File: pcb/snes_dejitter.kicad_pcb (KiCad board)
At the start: 2 copper layers, 44.1 x 23.7 mm, 39 parts, among them J1 JTAG_CONN, J10 CSYNC_o, J2 5V, J3 GND, J4 GND, J5 CSYNC_i, J6 MCLK_EXT_i, J7 CLK_SEL_i, J8 GND, J9 MCLK_o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

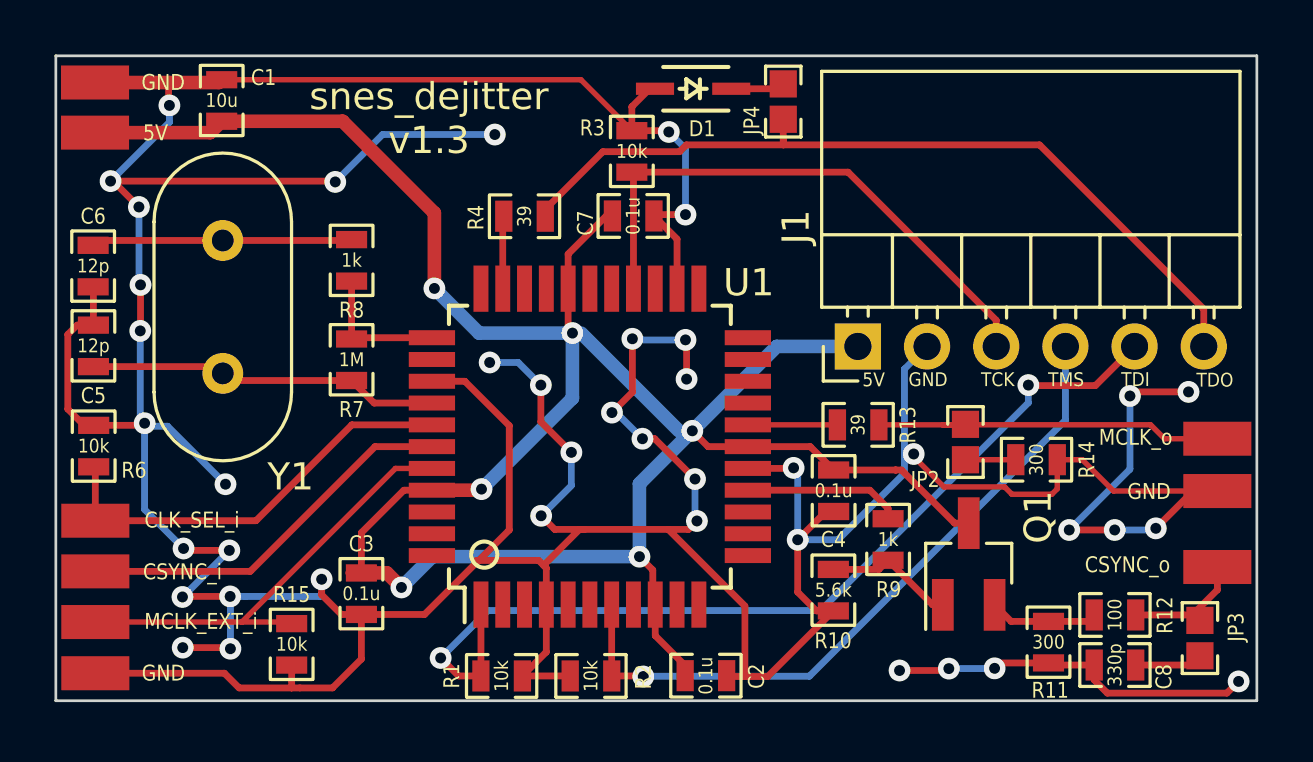
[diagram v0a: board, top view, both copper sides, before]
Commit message: update to ATF1502AS-10JU44
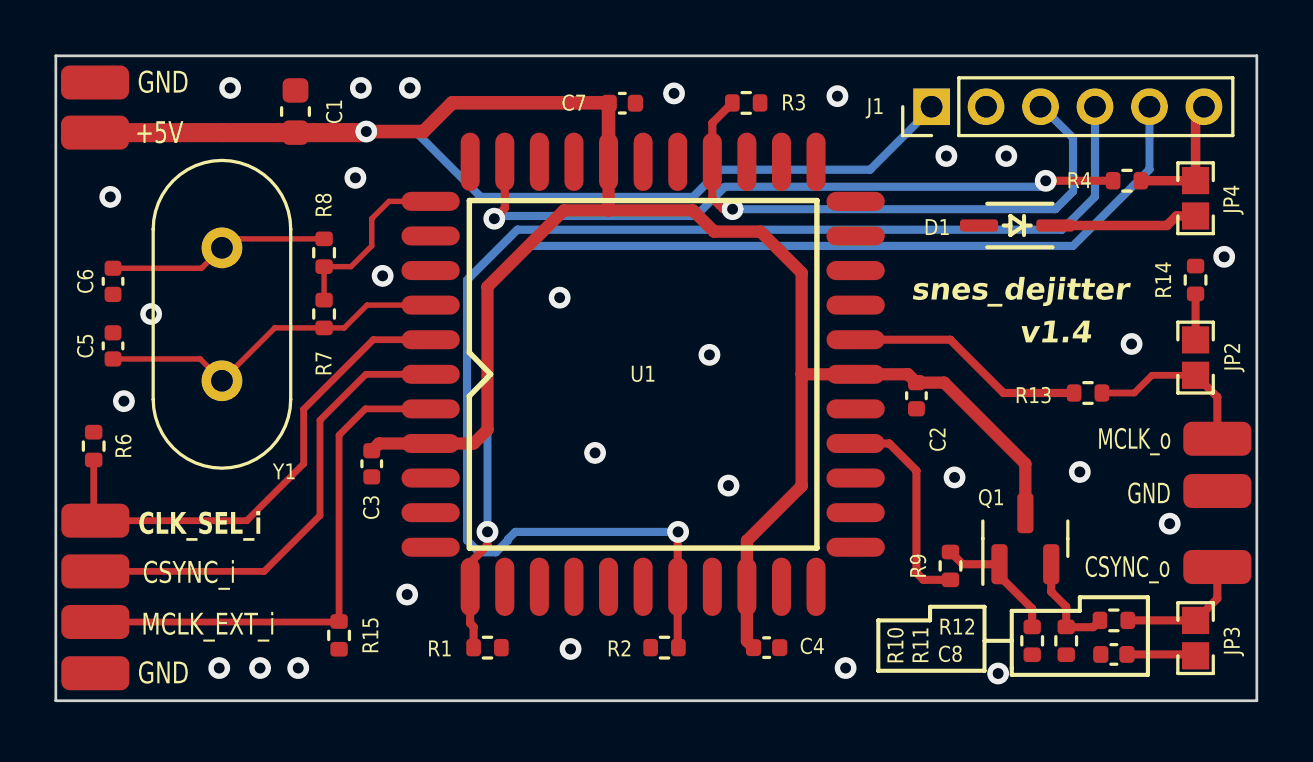
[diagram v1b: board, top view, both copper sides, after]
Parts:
- C1: footprint custom_components:SM0603_Capa_libcms -> Capacitor_SMD:C_0603_1608Metric
- C2, C3, C4, C5, C6, C7, C8: footprint custom_components:SM0603_Capa_libcms -> Capacitor_SMD:C_0402_1005Metric
- J1: footprint custom_components:JTAG_Header_Angled_1x06_Pitch2.54mm -> Connector_PinHeader_2.00mm:PinHeader_1x06_P2.00mm_Vertical
- J2: value 5V -> +5V
- Q1: footprint TO_SOT_Packages_SMD:SOT-23_Handsoldering -> Package_TO_SOT_SMD:SOT-23
- R1, R10, R11, R12, R13, R14, R15, R2, R3, R4, R6, R7, R8, R9: footprint custom_components:SM0603_Resistor_libcms -> Resistor_SMD:R_0402_1005Metric
- U1: footprint custom_components:TQFP-44_10x10mm_Pitch0.8mm_Handsoldering -> SamacSys_Parts:PLCC127P1753X1753X457-44N
- moved R4 22.2 mm to (52.2, 17.6)
- moved JP4 15.6 mm to (54.8, 18.2), turned to -90 degrees
- moved D1 12.9 mm to (48.2, 19.2)
- moved C2 12.9 mm to (44.5, 25.5), turned to -90 degrees
- moved J1 9.21 mm to (45.1, 14.9)
- moved JP2 9.00 mm to (54.8, 24.1), turned to 90 degrees
- moved R14 8.81 mm to (54.8, 21.2), turned to 90 degrees
- moved R13 8.52 mm to (50.8, 25.4)
- moved R10 7.53 mm to (48.8, 34.5)
- moved C4 6.26 mm to (39.0, 34.8), turned to 0 degrees
- moved C3 4.79 mm to (24.5, 28.0)
- moved R3 4.56 mm to (38.2, 14.8), turned to 0 degrees
- moved C7 4.16 mm to (33.7, 14.8)
- moved U1 3.30 mm to (34.5, 24.7)
- moved R2 2.89 mm to (35.2, 34.8)
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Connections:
- U1 pad 10: Net-(U1-Pad10) -> unconnected-(U1-Pad10)
- U1 pad 11: Net-(U1-Pad11) -> unconnected-(U1-Pad11)
- U1 pad 12: Net-(U1-Pad12) -> unconnected-(U1-Pad12)
- U1 pad 13: Net-(U1-Pad13) -> unconnected-(U1-Pad13)
- U1 pad 14: Net-(U1-Pad14) -> unconnected-(U1-Pad14)
- U1 pad 19: Net-(U1-Pad19) -> unconnected-(U1-Pad19)
- U1 pad 2: Net-(U1-Pad2) -> unconnected-(U1-Pad2)
- U1 pad 20: Net-(U1-Pad20) -> unconnected-(U1-Pad20)
- U1 pad 21: Net-(U1-Pad21) -> unconnected-(U1-Pad21)
- U1 pad 22: Net-(U1-Pad22) -> unconnected-(U1-Pad22)
- U1 pad 23: Net-(U1-Pad23) -> unconnected-(U1-Pad23)
- U1 pad 25: Net-(U1-Pad25) -> unconnected-(U1-Pad25)
- U1 pad 27: Net-(U1-Pad27) -> unconnected-(U1-Pad27)
- U1 pad 28: Net-(U1-Pad28) -> unconnected-(U1-Pad28)
- U1 pad 3: Net-(U1-Pad3) -> unconnected-(U1-Pad3)
- U1 pad 30: Net-(U1-Pad30) -> unconnected-(U1-Pad30)
- U1 pad 31: Net-(U1-Pad31) -> unconnected-(U1-Pad31)
- U1 pad 33: Net-(U1-Pad33) -> unconnected-(U1-Pad33)
- U1 pad 35: Net-(U1-Pad35) -> unconnected-(U1-Pad35)
- U1 pad 42: Net-(U1-Pad42) -> unconnected-(U1-Pad42)
- U1 pad 43: Net-(U1-Pad43) -> unconnected-(U1-Pad43)
- U1 pad 44: Net-(U1-Pad44) -> unconnected-(U1-Pad44)
- U1 pad 5: Net-(U1-Pad5) -> unconnected-(U1-Pad5)
- U1 pad 6: Net-(U1-Pad6) -> unconnected-(U1-Pad6)
- U1 pad 8: Net-(U1-Pad8) -> unconnected-(U1-Pad8)
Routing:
- net GND: track 230.1 -> 0.00 mm, vias 41 -> 28
- net Net-(J1-Pad6): track 30.2 -> 4.95 mm
- net /TMS: track 25.9 -> 49.7 mm
- net /TDO: track 2.68 -> 25.5 mm, vias 0 -> 2
- net /DVDD5V: track 88.4 -> 96.0 mm, vias 6 -> 1
- net Net-(R13-Pad1): track 13.5 -> 6.37 mm
- net /TDI: track 35.0 -> 42.0 mm, vias 2 -> 1
- net /GCLK_o: track 3.29 -> 8.83 mm
- net Net-(JP4-Pad2): track 1.98 -> 5.54 mm
- net /CSYNC_i: track 14.3 -> 17.4 mm
- net /MCLK_EXT_i: track 16.8 -> 19.5 mm
- net /MCLK_SEL_i: track 15.8 -> 18.2 mm
- net /CSYNC_o: track 5.81 -> 7.75 mm
- net Net-(U1-Pad34): track 5.10 -> 6.72 mm
- net Net-(C6-Pad1): track 9.58 -> 8.20 mm
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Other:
- net class Default removed
- board text added: "snes_dejitter"
- board text added: "v1.4"
- board text removed: "snes_dejitter v1.3"
